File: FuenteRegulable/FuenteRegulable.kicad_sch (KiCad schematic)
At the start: 3 parts, among them J1 AC_IN, J2 T_IN, J3 T_OUT

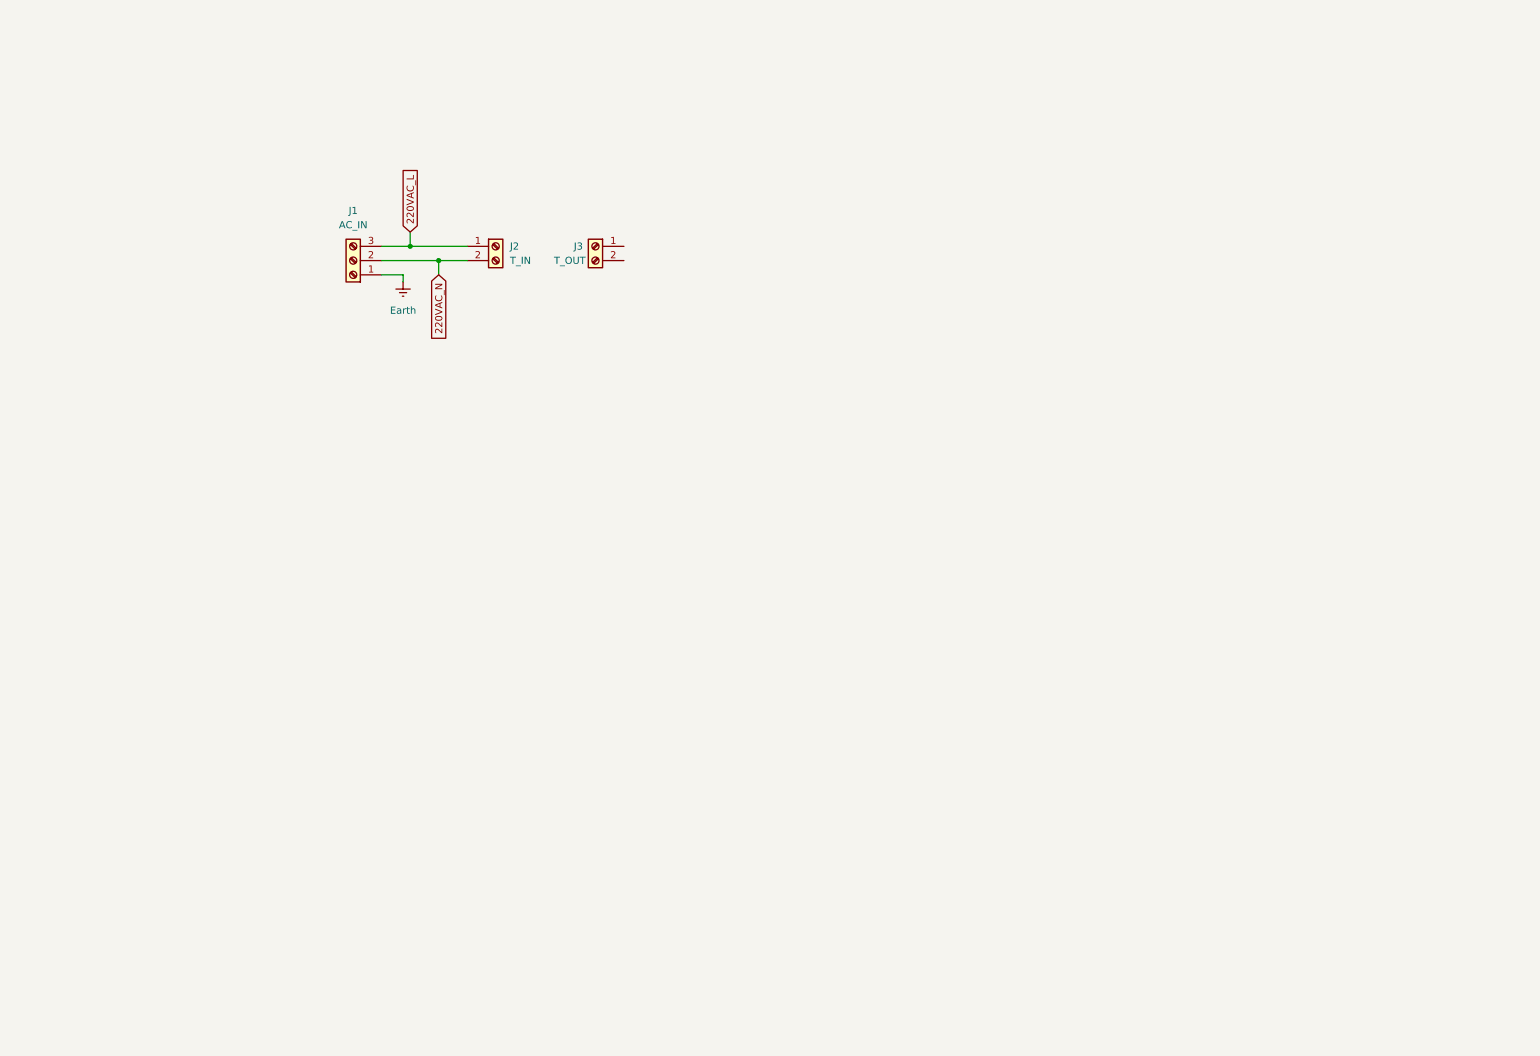
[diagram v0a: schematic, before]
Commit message: Diagrama esquematico terminado
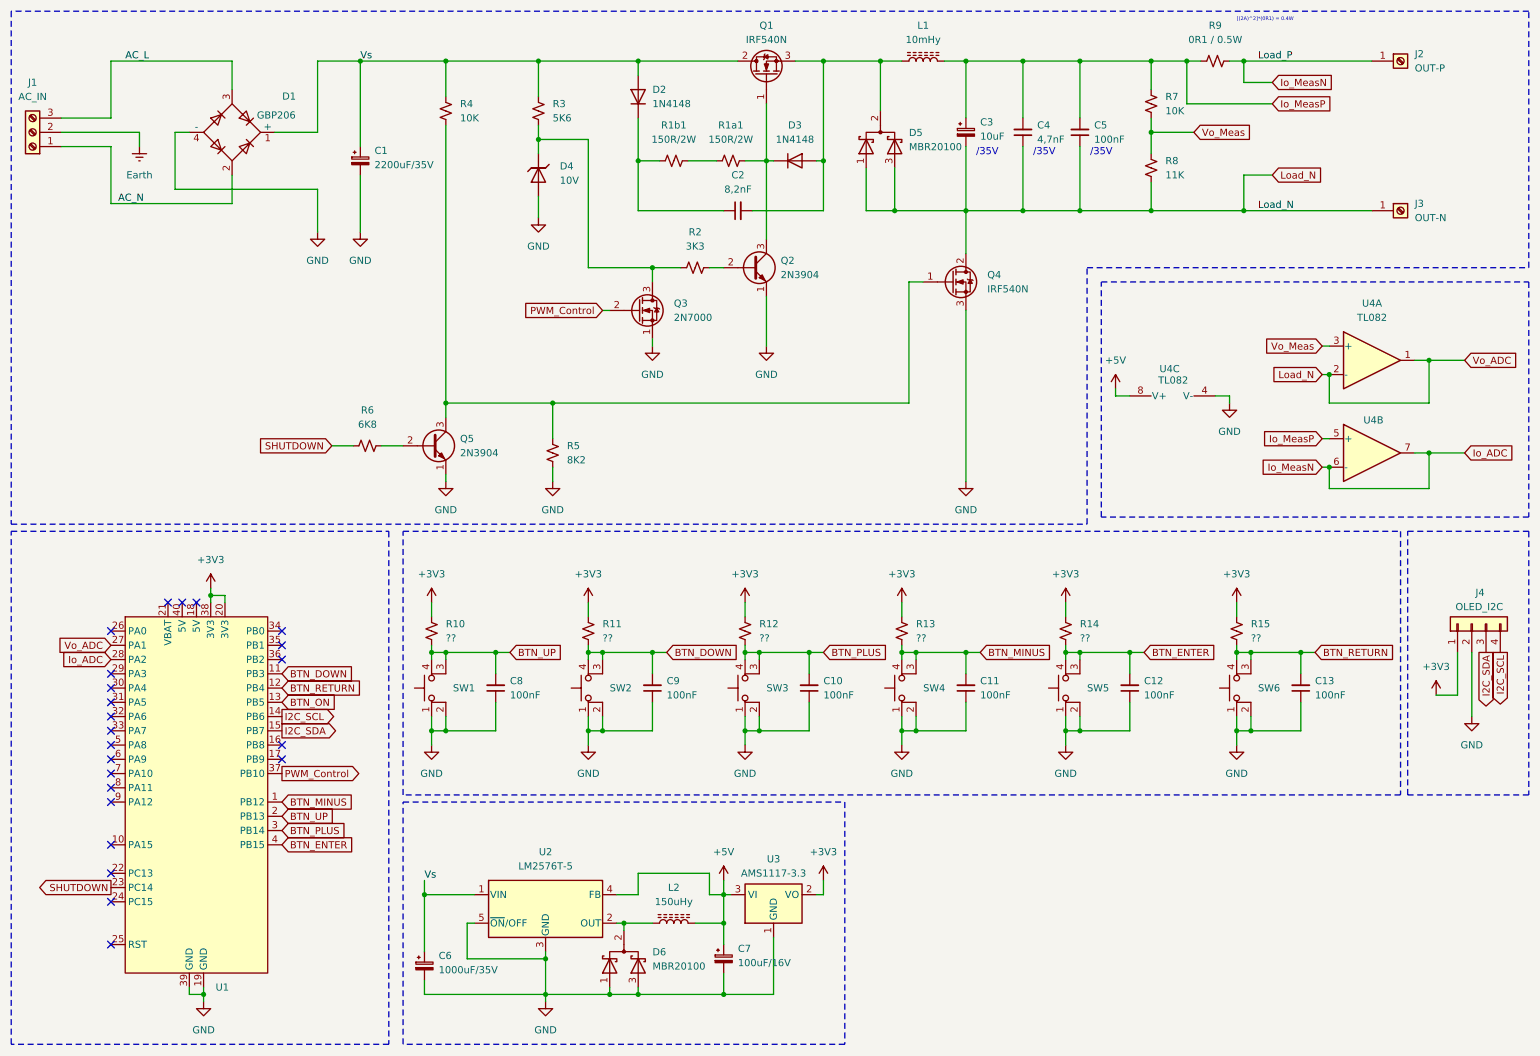
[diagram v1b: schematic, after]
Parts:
- removed J2: T_IN, TerminalBlock_Phoenix:TerminalBlock_Phoenix_MKDS-1,5-2-5.08_1x02_P5.08mm_Horizontal, symbol Connector:Screw_Terminal_01x02
- removed J3: T_OUT, TerminalBlock_Phoenix:TerminalBlock_Phoenix_MKDS-1,5-2-5.08_1x02_P5.08mm_Horizontal, symbol Connector:Screw_Terminal_01x02
- added C1: 2200uF/35V, Capacitor_THT:CP_Radial_D16.0mm_P7.50mm, symbol Device:C_Polarized_Small
- added C10, C11, C12, C13, C5, C8, C9: 100nF, Capacitor_THT:C_Disc_D3.0mm_W2.0mm_P2.50mm, symbol Device:C_Small
- added C2: 8,2nF, Capacitor_THT:C_Disc_D3.0mm_W2.0mm_P2.50mm, symbol Device:C_Small
- added C3: 10uF, Capacitor_THT:CP_Radial_D4.0mm_P2.00mm, symbol Device:C_Polarized_Small
- added C4: 4,7nF, Capacitor_THT:C_Rect_L7.0mm_W2.0mm_P5.00mm, symbol Device:C_Small
- added C6: 1000uF/35V, Capacitor_THT:CP_Radial_D14.0mm_P7.50mm, symbol Device:C_Polarized_Small
- added C7: 100uF/16V, Capacitor_THT:CP_Radial_D8.0mm_P5.00mm, symbol Device:C_Polarized_Small
- added D1: GBP206, Diode_THT:Diode_Bridge_32.0x5.6x17.0mm_P10.0mm_P7.5mm, symbol Diode_Bridge:KBU6A
- added D2, D3: 1N4148, Diode_THT:D_DO-35_SOD27_P7.62mm_Horizontal, symbol Diode:1N4148
- added D4: 10V, Diode_THT:D_DO-41_SOD81_P10.16mm_Horizontal, symbol Device:D_Zener
- added D5, D6: MBR20100, Package_TO_SOT_THT:TO-220-3_Vertical, symbol Device:D_Schottky_Dual_CommonCathode_AKA_Parallel
- added J2: OUT-P, Connector_Wire:SolderWirePad_1x01_SMD_5x10mm, symbol Connector:Screw_Terminal_01x01
- added J3: OUT-N, Connector_Wire:SolderWirePad_1x01_SMD_5x10mm, symbol Connector:Screw_Terminal_01x01
- added J4: OLED_I2C, Connector_PinSocket_2.54mm:PinSocket_1x04_P2.54mm_Vertical, symbol Connector_Generic:Conn_01x04
- added L1: 10mHy, Inductor_THT:L_Toroid_Vertical_L16.0mm_W8.0mm_P7.62mm, symbol Device:L_Ferrite
- added L2: 150uHy, Inductor_THT:L_Toroid_Vertical_L16.0mm_W8.0mm_P7.62mm, symbol Device:L_Ferrite
- added Q1, Q4: IRF540N, Package_TO_SOT_THT:TO-220-3_Vertical, symbol Transistor_FET:IRF540N
- added Q2, Q5: 2N3904, Package_TO_SOT_THT:TO-92_Wide, symbol Transistor_BJT:2N3904
- added Q3: 2N7000, Package_TO_SOT_THT:TO-92_Wide, symbol Transistor_FET:2N7000
- added R10, R11, R12, R13, R14, R15: ??, Resistor_THT:R_Axial_DIN0207_L6.3mm_D2.5mm_P7.62mm_Horizontal, symbol Device:R_Small_US
- added R1a1, R1b1: 150R/2W, Resistor_THT:R_Axial_DIN0614_L14.3mm_D5.7mm_P15.24mm_Horizontal, symbol Device:R_Small_US
- added R2: 3K3, Resistor_THT:R_Axial_DIN0207_L6.3mm_D2.5mm_P7.62mm_Horizontal, symbol Device:R_Small_US
- added R3: 5K6, Resistor_THT:R_Axial_DIN0207_L6.3mm_D2.5mm_P7.62mm_Horizontal, symbol Device:R_Small_US
- added R4, R7: 10K, Resistor_THT:R_Axial_DIN0207_L6.3mm_D2.5mm_P7.62mm_Horizontal, symbol Device:R_Small_US
- added R5: 8K2, Resistor_THT:R_Axial_DIN0207_L6.3mm_D2.5mm_P7.62mm_Horizontal, symbol Device:R_Small_US
- added R6: 6K8, Resistor_THT:R_Axial_DIN0207_L6.3mm_D2.5mm_P7.62mm_Horizontal, symbol Device:R_Small_US
- added R8: 11K, Resistor_THT:R_Axial_DIN0207_L6.3mm_D2.5mm_P7.62mm_Horizontal, symbol Device:R_Small_US
- added R9: 0R1 / 0.5W, Resistor_THT:R_Axial_DIN0411_L9.9mm_D3.6mm_P12.70mm_Horizontal, symbol Device:R_Small_US
- added SW1, SW2, SW3, SW4, SW5, SW6: SW_MEC_5E, Button_Switch_SMD:SW_MEC_5GSH9, symbol Switch:SW_MEC_5E
- added U1: ~, STM32:STM32BlackPill, symbol Project_Library:STM32BlackPill
- added U2: LM2576T-5, Package_TO_SOT_THT:TO-220-5_Vertical, symbol Regulator_Switching:LM2576T-5
- added U3: AMS1117-3.3, Package_TO_SOT_SMD:SOT-223-3_TabPin2, symbol Regulator_Linear:AMS1117-3.3
- added U4: TL082, Package_DIP:DIP-8_W7.62mm, symbol Amplifier_Operational:TL082
- J1: footprint TerminalBlock_MetzConnect:TerminalBlock_MetzConnect_Type171_RT13703HBWC_1x03_P7.50mm_Horizontal -> TerminalBlock_Phoenix:TerminalBlock_Phoenix_MKDS-1,5-3-5.08_1x03_P5.08mm_Horizontal
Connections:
- net 220VAC_N is gone; now on net Earth: J1.2 (Pin_2)
- net Earth: no longer J1.1 (Pin_1)
- net 220VAC_L renamed AC_L
- net AC_L: now also D1.3
- new net: D4.1 (K), Q3.3 (D), R2.1, R3.1
- new net: D3.1 (K), Q1.1 (G), Q2.3 (C), R1a1.2
- new net: C2.2, D3.2 (A), D5.2 (K), L1.1, Q1.3 (S)
- new net: C2.1, D2.1 (K), R1b1.1
- new net: Q4.1 (G), Q5.3 (C), R4.1, R5.2
- new net: R1a1.1, R1b1.2
- new net: Q5.2 (B), R6.2
- new net: D6.2 (K), L2.1, U2.2 (OUT)
- new net: Q2.2 (B), R2.2
- new net +3V3: J4.1 (Pin_1), R10.2, R11.2, R12.2, R13.2, R14.2, R15.2, U1.20 (3V3), U1.38 (3V3), U3.2 (VO)
- new net +5V: C7.1, L2.2, U2.4 (FB), U3.3 (VI), U4.8 (V+)
- new net AC_N: D1.2, J1.1 (Pin_1)
- new net BTN_DOWN: C9.2, R11.1, SW2.3 (K), SW2.4 (A), U1.11 (PB3)
- new net BTN_ENTER: C12.2, R14.1, SW5.3 (K), SW5.4 (A), U1.4 (PB15)
- new net BTN_MINUS: C11.2, R13.1, SW4.3 (K), SW4.4 (A), U1.1 (PB12)
- new net BTN_ON: U1.13 (PB5)
- new net BTN_PLUS: C10.2, R12.1, SW3.3 (K), SW3.4 (A), U1.3 (PB14)
- new net BTN_RETURN: C13.2, R15.1, SW6.3 (K), SW6.4 (A), U1.12 (PB4)
- new net BTN_UP: C8.2, R10.1, SW1.3 (K), SW1.4 (A), U1.2 (PB13)
- new net GND: C1.2, C10.1, C11.1, C12.1, C13.1, C6.2, C7.2, C8.1, C9.1, D1.4 (-), D4.2 (A), D6.1 (A), D6.3 (A), J4.2 (Pin_2), Q2.1 (E), Q3.1 (S), Q4.3 (S), Q5.1 (E), R5.1, SW1.1, SW1.2, SW2.1, SW2.2, SW3.1, SW3.2, SW4.1, SW4.2, SW5.1, SW5.2, SW6.1, SW6.2, U1.19 (GND), U1.39 (GND), U2.3 (GND), U2.5 (~{ON}/OFF), U3.1 (GND), U4.4 (V-)
- new net I2C_SCL: J4.4 (Pin_4), U1.14 (PB6)
- new net I2C_SDA: J4.3 (Pin_3), U1.15 (PB7)
- new net Io_ADC: J2.1 (Pin_1), R9.1, U1.28 (PA2), U4.6 (-), U4.7
- new net Io_MeasP: C3.1, C4.2, C5.2, L1.2, R7.2, R9.2, U4.5 (+)
- new net Load_N: C3.2, C4.1, C5.1, D5.1 (A), D5.3 (A), J3.1 (Pin_1), Q4.2 (D), R8.1, U1.27 (PA1), U4.1, U4.2 (-)
- new net PWM_Control: Q3.2 (G), U1.37 (PB10)
- new net SHUTDOWN: R6.1, U1.23 (PC14)
- new net Vo_Meas: R7.1, R8.2, U4.3 (+)
- new net Vs: C1.1, C6.1, D1.1 (+), D2.2 (A), Q1.2 (D), R3.2, R4.2, U2.1 (VIN)
- no-connect marks 0 -> 23
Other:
- note added: "/35V"
- note added: "[(2A)^2]*(0R1) = 0.4W"

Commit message: Comienzo a rutear PCB
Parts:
- D5, D6: footprint Package_TO_SOT_THT:TO-220-3_Vertical -> Package_TO_SOT_THT:TO-220-3_Horizontal_TabDown
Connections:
- net +3V3: now also J4.2 (Pin_2); no longer J4.1 (Pin_1)
- net GND: now also J4.1 (Pin_1); no longer J4.2 (Pin_2)
- net I2C_SCL: now also J4.3 (Pin_3); no longer J4.4 (Pin_4)
- net I2C_SDA: now also J4.4 (Pin_4); no longer J4.3 (Pin_3)
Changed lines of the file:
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@@
 	)
 	(no_connect
+		(at 43.18 118.11)
+	)
+	(no_connect
 		(at 60.96 123.19)
 	)
@@
 	)
 	(no_connect
-		(at 43.18 118.11)
-	)
-	(no_connect
 		(at 30.48 135.89)
 	)
@@
 	(wire
 		(pts
-			(xy 273.05 138.43) (xy 273.05 127)
+			(xy 273.05 127) (xy 273.05 146.05)
 		)
 		(stroke
@@
 	(wire
 		(pts
-			(xy 266.7 134.62) (xy 270.51 134.62)
+			(xy 266.7 128.27) (xy 270.51 128.27)
 		)
 		(stroke
@@
 	(wire
 		(pts
+			(xy 266.7 146.05) (xy 273.05 146.05)
+		)
+		(stroke
+			(width 0)
+			(type default)
+		)
+	)
+	(wire
+		(pts
 			(xy 215.9 43.18) (xy 215.9 48.26)
 		)
@@
 	(wire
 		(pts
+			(xy 266.7 143.51) (xy 266.7 146.05)
+		)
+		(stroke
+			(width 0)
+			(type default)
+		)
+	)
+	(wire
+		(pts
 			(xy 265.43 91.44) (xy 271.78 91.44)
 		)
@@
 	(wire
 		(pts
-			(xy 270.51 134.62) (xy 270.51 127)
+			(xy 270.51 128.27) (xy 270.51 127)
 		)
 		(stroke
@@
 	(wire
 		(pts
+			(xy 266.7 128.27) (xy 266.7 129.54)
+		)
+		(stroke
+			(width 0)
+			(type default)
+		)
+	)
+	(wire
+		(pts
 			(xy 87.63 140.97) (xy 87.63 143.51)
 		)
@@
 		)
 	)
-	(global_label "I2C_SCL"
-		(shape output)
-		(at 278.13 127 270)
-		(fields_autoplaced yes)
-		(effects
-			(font
-				(size 1.27 1.27)
-			)
-			(justify right)
-		)
-		(property "Intersheetrefs" "${INTERSHEET_REFS}"
-			(at 278.13 137.5447 90)
-			(effects
-				(font
-					(size 1.27 1.27)
-				)
-				(justify right)
-				(hide yes)
-			)
-		)
-	)
 	(global_label "Io_MeasP"
 		(shape input)
@@
 		)
 	)
-	(global_label "I2C_SDA"
-		(shape output)
-		(at 275.59 127 270)
+	(global_label "Vo_ADC"
+		(shape input)
+		(at 30.48 125.73 180)
 		(fields_autoplaced yes)
 		(effects
@@
 		)
 		(property "Intersheetrefs" "${INTERSHEET_REFS}"
-			(at 275.59 137.6052 90)
+			(at 20.661 125.73 0)
 			(effects
 				(font
@@
 		)
 	)
-	(global_label "Vo_ADC"
-		(shape input)
-		(at 30.48 125.73 180)
+	(global_label "I2C_SDA"
+		(shape output)
+		(at 60.96 140.97 0)
 		(fields_autoplaced yes)
 		(effects
@@
 				(size 1.27 1.27)
 			)
-			(justify right)
+			(justify left)
 		)
 		(property "Intersheetrefs" "${INTERSHEET_REFS}"
-			(at 20.661 125.73 0)
+			(at 71.5652 140.97 0)
 			(effects
 				(font
 					(size 1.27 1.27)
 				)
-				(justify right)
+				(justify left)
 				(hide yes)
 			)
@@
 	(global_label "I2C_SDA"
 		(shape output)
-		(at 60.96 140.97 0)
+		(at 278.13 127 270)
 		(fields_autoplaced yes)
 		(effects
@@
 				(size 1.27 1.27)
 			)
-			(justify left)
+			(justify right)
 		)
 		(property "Intersheetrefs" "${INTERSHEET_REFS}"
-			(at 71.5652 140.97 0)
+			(at 278.13 137.6052 90)
 			(effects
 				(font
 					(size 1.27 1.27)
 				)
-				(justify left)
+				(justify right)
 				(hide yes)
 			)
@@
 		)
 	)
+	(global_label "I2C_SCL"
+		(shape output)
+		(at 275.59 127 270)
+		(fields_autoplaced yes)
+		(effects
+			(font
+				(size 1.27 1.27)
+			)
+			(justify right)
+		)
+		(property "Intersheetrefs" "${INTERSHEET_REFS}"
+			(at 275.59 137.5447 90)
+			(effects
+				(font
+					(size 1.27 1.27)
+				)
+				(justify right)
+				(hide yes)
+			)
+		)
+	)
 	(global_label "BTN_PLUS"
 		(shape input)
@@
 	(symbol
 		(lib_id "power:GND")
-		(at 273.05 138.43 0)
+		(at 266.7 129.54 0)
 		(unit 1)
 		(exclude_from_sim no)
@@
 		(dnp no)
 		(property "Reference" "#PWR020"
-			(at 273.05 144.78 0)
+			(at 266.7 135.89 0)
 			(effects
 				(font
@@
 		)
 		(property "Value" "GND"
-			(at 273.05 143.51 0)
+			(at 266.7 134.62 0)
 			(effects
 				(font
@@
 		)
 		(property "Footprint" ""
-			(at 273.05 138.43 0)
+			(at 266.7 129.54 0)
 			(effects
 				(font
@@
 		)
 		(property "Datasheet" ""
-			(at 273.05 138.43 0)
+			(at 266.7 129.54 0)
 			(effects
 				(font
@@
 		)
 		(property "Description" "Power symbol creates a global label with name \"GND\" , ground"
-			(at 273.05 138.43 0)
+			(at 266.7 129.54 0)
 			(effects
 				(font
@@
 	)
 	(symbol
-		(lib_id "power:+3V3")
-		(at 266.7 134.62 0)
-		(unit 1)
-		(exclude_from_sim no)
-		(in_bom yes)
-		(on_board yes)
-		(dnp no)
-		(fields_autoplaced yes)
-		(property "Reference" "#PWR019"
-			(at 266.7 138.43 0)
-			(effects
-				(font
-					(size 1.27 1.27)
-				)
-				(hide yes)
-			)
-		)
-		(property "Value" "+3V3"
-			(at 266.7 129.54 0)
-			(effects
-				(font
-					(size 1.27 1.27)
-				)
-			)
-		)
-		(property "Footprint" ""
-			(at 266.7 134.62 0)
-			(effects
-				(font
-					(size 1.27 1.27)
-				)
-				(hide yes)
-			)
-		)
-		(property "Datasheet" ""
-			(at 266.7 134.62 0)
-			(effects
-				(font
-					(size 1.27 1.27)
-				)
-				(hide yes)
-			)
-		)
-		(property "Description" "Power symbol creates a global label with name \"+3V3\""
-			(at 266.7 134.62 0)
-			(effects
-				(font
-					(size 1.27 1.27)
-				)
-				(hide yes)
-			)
-		)
-		(pin "1"
-		)
-		(instances
-			(project "FuenteRegulable"
-				(path "/5147e114-c546-465f-ae8b-30b4dd1b416a"
-					(reference "#PWR019")
-					(unit 1)
-				)
-			)
-		)
-	)
-	(symbol
 		(lib_id "Device:R_Small_US")
 		(at 130.81 39.37 90)
@@
 			)
 		)
-		(property "Footprint" "Package_TO_SOT_THT:TO-220-3_Vertical"
+		(property "Footprint" "Package_TO_SOT_THT:TO-220-3_Horizontal_TabDown"
 			(at 167.64 34.29 0)
 			(effects
@@
 	)
 	(symbol
+		(lib_id "power:+3V3")
+		(at 266.7 143.51 0)
+		(unit 1)
+		(exclude_from_sim no)
+		(in_bom yes)
+		(on_board yes)
+		(dnp no)
+		(fields_autoplaced yes)
+		(property "Reference" "#PWR031"
+			(at 266.7 147.32 0)
+			(effects
+				(font
+					(size 1.27 1.27)
+				)
+				(hide yes)
+			)
+		)
+		(property "Value" "+3V3"
+			(at 266.7 138.43 0)
+			(effects
+				(font
+					(size 1.27 1.27)
+				)
+			)
+		)
+		(property "Footprint" ""
+			(at 266.7 143.51 0)
+			(effects
+				(font
+					(size 1.27 1.27)
+				)
+				(hide yes)
+			)
+		)
+		(property "Datasheet" ""
+			(at 266.7 143.51 0)
+			(effects
+				(font
+					(size 1.27 1.27)
+				)
+				(hide yes)
+			)
+		)
+		(property "Description" "Power symbol creates a global label with name \"+3V3\""
+			(at 266.7 143.51 0)
+			(effects
+				(font
+					(size 1.27 1.27)
+				)
+				(hide yes)
+			)
+		)
+		(pin "1"
+		)
+		(instances
+			(project "FuenteRegulable"
+				(path "/5147e114-c546-465f-ae8b-30b4dd1b416a"
+					(reference "#PWR031")
+					(unit 1)
+				)
+			)
+		)
+	)
+	(symbol
 		(lib_id "Connector_Generic:Conn_01x04")
 		(at 273.05 121.92 90)
@@
 			)
 		)
-		(property "Footprint" "Package_TO_SOT_THT:TO-220-3_Vertical"
+		(property "Footprint" "Package_TO_SOT_THT:TO-220-3_Horizontal_TabDown"
 			(at 121.92 180.34 0)
 			(effects
